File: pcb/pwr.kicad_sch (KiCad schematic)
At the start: 7 parts, among them U2 MCP73831-2-OT

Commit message: sussy
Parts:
- added BT2: Battery_Cell, symbol Device:Battery_Cell
- added C19: 10uF, symbol Device:C_Small
- added C20: 22uF, symbol Device:C_Small
- added C21, C22, C23: 1uF, symbol Device:C_Small
- added C24: 4.7uF, symbol Device:C_Small
- added D2: red, symbol Device:LED_Small
- added D3: green, symbol Device:LED_Small
- added L4: 0.47uH, symbol Device:L_Small
- added R10: 46.4k, symbol Device:R_Small
- added R11: 4.12k, symbol Device:R_Small
- added R12: 10k, symbol Device:R_Small
- added R3: 100k, symbol Device:R_Small
- added R4: 511k, symbol Device:R_Small
- added R5: 91k, symbol Device:R_Small
- added R6, R7: 1.5k, symbol Device:R_Small
- added R8: 1.18k, symbol Device:R_Small
- added R9: 1.13k, symbol Device:R_Small
- added U4: TPS63802DLAR, TPS63802DLAR:VREG_TPS63802DLAR, symbol TPS63802:TPS63802DLAR
- added U5: BQ24074RGT, Package_DFN_QFN:VQFN-16-1EP_3x3mm_P0.5mm_EP1.6x1.6mm, symbol Battery_Management:BQ24074RGT
- added U6: TPS7A20xxxDQN, Package_SON:Texas_X2SON-4_1x1mm_P0.65mm, symbol Regulator_Linear:TPS7A20xxxDQN
- BT1, C1, C16, D1, R1, R2, U2: now not fitted; now left out of the parts list
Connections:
- net GND: now also BT1.2 (-), C1.2, BT2.2 (-), C19.2, C20.2, C21.2, C22.2, C23.2, C24.2, R10.1, R11.1, R12.2, R5.2, R8.1, R9.1, U4.2 (MODE), U4.3 (AGND), U4.8 (GND), U5.17 (VSS), U5.8 (VSS), U6.2 (GND), U6.5 (Pad)
- net VBUS: now also C23.1, U5.13 (IN)
- net at R2.1, U2.5 (PROG): no longer R1.2
- net +BATT: now reaches BT1.1 (+), C1.1, U2.3 (V_{BAT})
- net +BATT: now also C19.1, R3.1, R6.2, R7.2, U4.10 (VIN), U5.10 (OUT), U5.11 (OUT)
- new net: D3.1 (K), U5.7 (~{PGOOD})
- new net: D3.2 (A), R6.1
- new net: R12.1, U5.1 (TS)
- new net: R10.2, U5.14 (TMR)
- new net: R4.2, R5.1, U4.4 (FB)
- new net: R3.2, U4.5 (PG)
- new net: L4.1, U4.7 (L2)
- new net: L4.2, U4.9 (L1)
- new net: D2.1 (K), U5.9 (~{CHG})
- new net: D2.2 (A), R7.1
- new net: R1.2, U2.1 (STAT)
- new net: R8.2, U5.12 (ILIM)
- new net: R11.2, U5.15 (ITERM)
- new net: R9.2, U5.16 (ISET)
- new net: BT2.1 (+), C24.1, U5.2 (BAT), U5.3 (BAT)
- new net +3V0_GPS: C22.1, U6.1 (OUT)
- new net +3V3_ALT: C20.1, C21.1, R4.1, U4.6 (VOUT), U6.4 (IN)
- new net P0.25: U4.1 (EN)
- new net P0.26: U6.3 (EN)
- new net P1.04: U5.4 (~{CE})
- new net P1.05: U5.6 (EN1)
- new net P1.06: U5.5 (EN2)

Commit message: stuff
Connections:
- net VBAT_RAW: now reaches BT2.1 (+), C24.1, U5.2 (BAT), U5.3 (BAT)
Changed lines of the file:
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@@
 	)
 	(junction
+		(at 53.34 96.52)
+		(diameter 0)
+		(color 0 0 0 0)
+	)
+	(junction
 		(at 110.49 96.52)
 		(diameter 0)
@@
 	)
 	(junction
-		(at 66.04 96.52)
-		(diameter 0)
-		(color 0 0 0 0)
-	)
-	(junction
 		(at 96.52 116.84)
 		(diameter 0)
@@
 		)
 	)
+	(global_label "VBAT_RAW"
+		(shape input)
+		(at 231.14 104.14 0)
+		(fields_autoplaced yes)
+		(effects
+			(font
+				(size 1.27 1.27)
+			)
+			(justify left)
+		)
+		(property "Intersheetrefs" "${INTERSHEET_REFS}"
+			(at 243.3176 104.14 0)
+			(hide yes)
+			(show_name no)
+			(do_not_autoplace no)
+			(effects
+				(font
+					(size 1.27 1.27)
+				)
+				(justify left)
+			)
+		)
+	)
 	(global_label "P0.25"
 		(shape input)
@@
 		(in_pos_files yes)
 		(dnp no)
-		(fields_autoplaced yes)
 		(property "Reference" "BT2"
-			(at 234.95 106.1084 0)
+			(at 233.68 106.68 0)
 			(show_name no)
 			(do_not_autoplace no)
@@
 		)
 		(property "Value" "Battery_Cell"
-			(at 234.95 108.6484 0)
+			(at 233.68 109.22 0)
 			(show_name no)
 			(do_not_autoplace no)
@@
 	(symbol
 		(lib_id "power:+BATT")
-		(at 66.04 96.52 0)
+		(at 53.34 96.52 0)
 		(unit 1)
 		(body_style 1)
@@
 		(fields_autoplaced yes)
 		(property "Reference" "#PWR025"
-			(at 66.04 100.33 0)
+			(at 53.34 100.33 0)
 			(hide yes)
 			(show_name no)
@@
 		)
 		(property "Value" "+BATT"
-			(at 66.04 91.44 0)
+			(at 53.34 91.44 0)
 			(show_name no)
 			(do_not_autoplace no)
@@
 		)
 		(property "Footprint" ""
-			(at 66.04 96.52 0)
+			(at 53.34 96.52 0)
 			(hide yes)
 			(show_name no)
@@
 		)
 		(property "Datasheet" ""
-			(at 66.04 96.52 0)
+			(at 53.34 96.52 0)
 			(hide yes)
 			(show_name no)
@@
 		)
 		(property "Description" "Power symbol creates a global label with name \"+BATT\""
-			(at 66.04 96.52 0)
+			(at 53.34 96.52 0)
 			(hide yes)
 			(show_name no)

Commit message: sus commit
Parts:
- BT2: footprint (none) -> Connector_JST:JST_PH_S2B-PH-SM4-TB_1x02-1MP_P2.00mm_Horizontal
- C19: footprint (none) -> Capacitor_SMD:C_0603_1608Metric; LCSC Part (none) -> C96446
- C20: footprint (none) -> Capacitor_SMD:C_0805_2012Metric; LCSC Part (none) -> C45783
- C21, C22, C23: footprint (none) -> Capacitor_SMD:C_0402_1005Metric; LCSC Part (none) -> C52923
- C24: footprint (none) -> Capacitor_SMD:C_0603_1608Metric; LCSC Part (none) -> C19666
- D2: footprint (none) -> LED_SMD:LED_0603_1608Metric; LCSC Part (none) -> C2286
- D3: footprint (none) -> LED_SMD:LED_0805_2012Metric; LCSC Part (none) -> C2297
- L4: footprint (none) -> JLCImport:XFL4015-471MEC
- R10: value 46.4k -> 1.18k; footprint (none) -> Resistor_SMD:R_0402_1005Metric; LCSC Part (none) -> C3016052
- R11: value 4.12k -> 1.13k; footprint (none) -> Resistor_SMD:R_0603_1608Metric; LCSC Part (none) -> C22833
- R12: value 10k -> 46.4k; footprint (none) -> Resistor_SMD:R_0402_1005Metric; LCSC Part (none) -> C5126026
- R3: footprint (none) -> Resistor_SMD:R_0402_1005Metric; LCSC Part (none) -> C25741
- R4: footprint (none) -> Resistor_SMD:R_0603_1608Metric; LCSC Part (none) -> C2930114
- R5: footprint (none) -> Resistor_SMD:R_0402_1005Metric; LCSC Part (none) -> C2906973
- R6, R7: footprint (none) -> Resistor_SMD:R_0402_1005Metric; LCSC Part (none) -> C25867
- R8: value 1.18k -> 1.5k; footprint (none) -> Resistor_SMD:R_0402_1005Metric; LCSC Part (none) -> C25867
- R9: value 1.13k -> 1.5k; footprint (none) -> Resistor_SMD:R_0402_1005Metric; LCSC Part (none) -> C25867
- U4: value TPS63802DLAR -> nRF52840; footprint TPS63802DLAR:VREG_TPS63802DLAR -> Package_DFN_QFN:Nordic_AQFN-73-1EP_7x7mm_P0.5mm; LCSC Part (none) -> C190794; MANUFACTURER Texas Instruments -> (none); MAXIMUM_PACKAGE_HEIGHT 1.0 mm -> (none); PARTREV B -> (none); STANDARD Manufacturer Recommendations -> (none)
- U5: value BQ24074RGT -> MAX-M10S; footprint Package_DFN_QFN:VQFN-16-1EP_3x3mm_P0.5mm_EP1.6x1.6mm -> RF_GPS:ublox_MAX; LCSC Part (none) -> C4153167
- U6: value TPS7A20xxxDQN -> TPS63802DLAR; footprint Package_SON:Texas_X2SON-4_1x1mm_P0.65mm -> TPS63802DLAR:VREG_TPS63802DLAR; LCSC Part (none) -> C2845237; MANUFACTURER (none) -> Texas Instruments; MAXIMUM_PACKAGE_HEIGHT (none) -> 1.0 mm; PARTREV (none) -> B; STANDARD (none) -> Manufacturer Recommendations

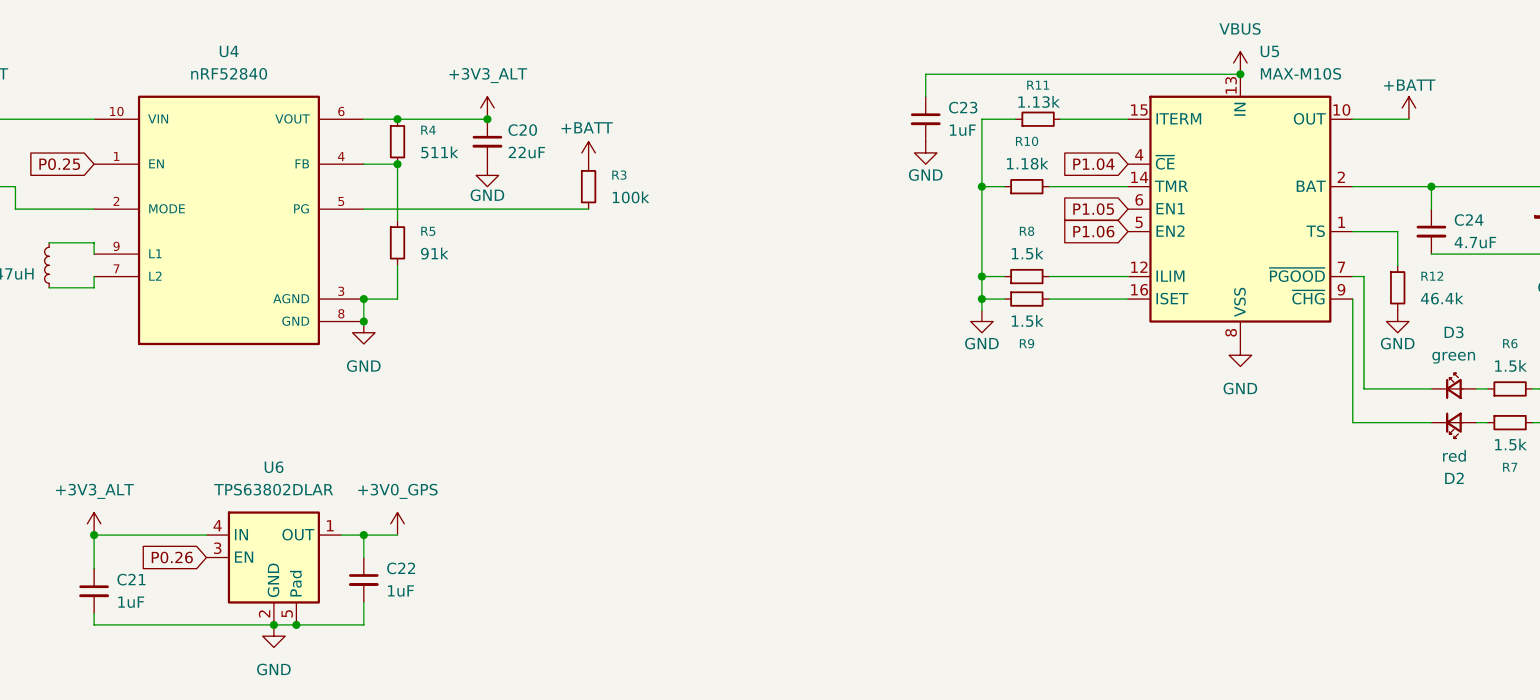
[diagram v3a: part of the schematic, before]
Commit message: fix symbols getting absolutely goofed up
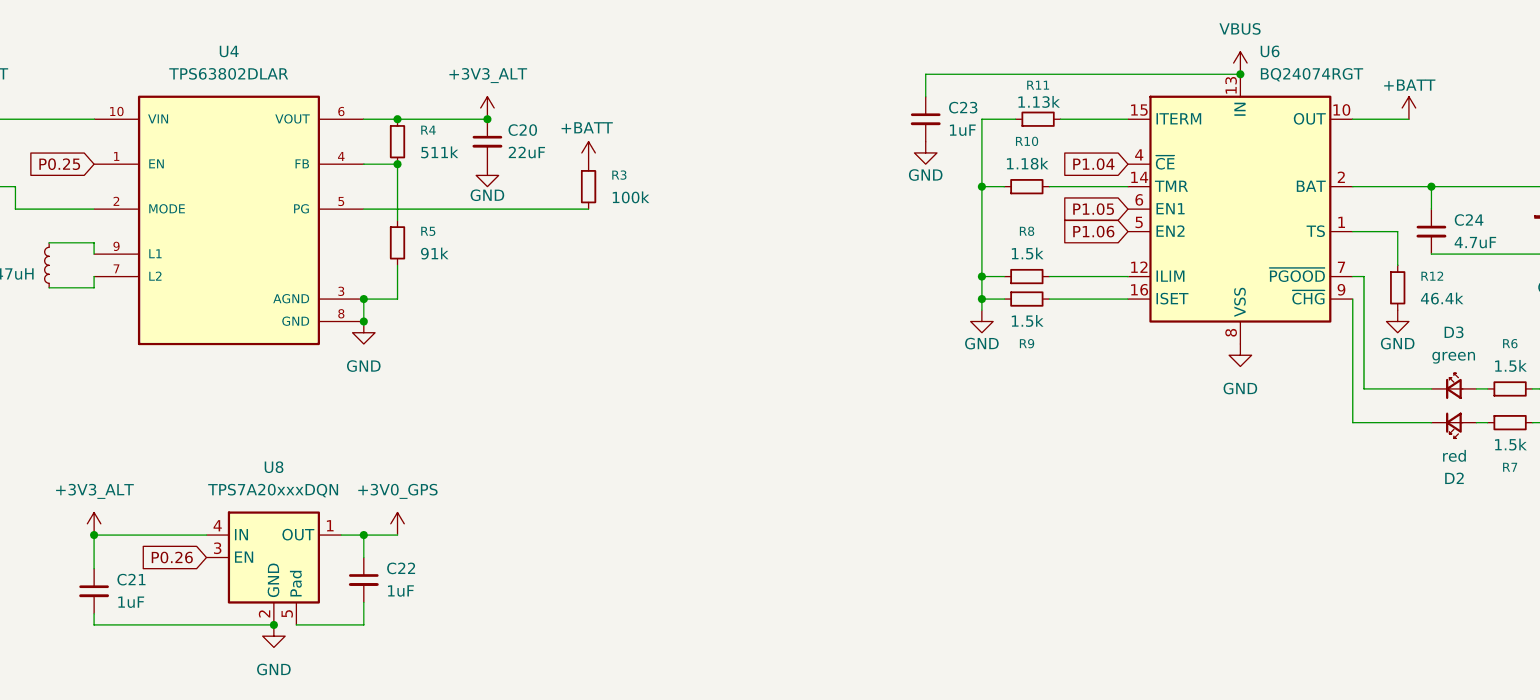
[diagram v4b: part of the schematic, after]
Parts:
- removed U5: MAX-M10S, RF_GPS:ublox_MAX, symbol Battery_Management:BQ24074RGT
- removed U6: TPS63802DLAR, TPS63802DLAR:VREG_TPS63802DLAR, symbol Regulator_Linear:TPS7A20xxxDQN
- added U6: BQ24074RGT, Package_DFN_QFN:VQFN-16-1EP_3x3mm_P0.5mm_EP1.6x1.6mm, symbol Battery_Management:BQ24074RGT
- added U8: TPS7A20xxxDQN, Package_SON:Texas_X2SON-4_1x1mm_P0.65mm, symbol Regulator_Linear:TPS7A20xxxDQN
- U4: value nRF52840 -> TPS63802DLAR; footprint Package_DFN_QFN:Nordic_AQFN-73-1EP_7x7mm_P0.5mm -> TPS63802DLAR:VREG_TPS63802DLAR; LCSC Part C190794 -> (none); MANUFACTURER (none) -> Texas Instruments; MAXIMUM_PACKAGE_HEIGHT (none) -> 1.0 mm; PARTREV (none) -> B; STANDARD (none) -> Manufacturer Recommendations
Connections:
- net +3V0_GPS: now also U8.1 (OUT)
- net +3V3_ALT: now also U8.4 (IN)
- net +BATT: now also U6.10 (OUT), U6.11 (OUT)
- net GND: now also U6.17 (VSS), U6.8 (VSS), U8.2 (GND); no longer C22.2
- net P0.26: now also U8.3 (EN)
- net P1.04: now also U6.4 (~{CE})
- net P1.05: now also U6.6 (EN1)
- net P1.06: now also U6.5 (EN2)
- net VBAT_RAW: now also U6.2 (BAT), U6.3 (BAT)
- net VBUS: now also U6.13 (IN)
- net at D3.1 (K): now also U6.7 (~{PGOOD})
- net at R12.1: now also U6.1 (TS)
- net at R10.2: now also U6.14 (TMR)
- net at D2.1 (K): now also U6.9 (~{CHG})
- net at R8.2: now also U6.12 (ILIM)
- net at R11.2: now also U6.15 (ITERM)
- net at R9.2: now also U6.16 (ISET)
- new net: C22.2, U8.5 (Pad)

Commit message: ALMOST done with parts purgatory
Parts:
- BT2: LCSC Part (none) -> C295747
- U4: LCSC Part (none) -> C2845237
- U6: LCSC Part (none) -> C54313
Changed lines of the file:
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@@
 			)
 		)
+		(property "LCSC Part" "C54313"
+			(at 195.58 106.68 0)
+			(hide yes)
+			(show_name no)
+			(do_not_autoplace no)
+			(effects
+				(font
+					(size 1.27 1.27)
+				)
+			)
+		)
 		(pin "11"
 		)
@@
 			)
 		)
+		(property "LCSC Part" "C2845237"
+			(at 81.28 106.68 0)
+			(hide yes)
+			(show_name no)
+			(do_not_autoplace no)
+			(effects
+				(font
+					(size 1.27 1.27)
+				)
+			)
+		)
 		(pin "9"
 		)
@@
 			(at 231.14 109.22 0)
 			(hide yes)
+			(show_name no)
+			(do_not_autoplace no)
+			(effects
+				(font
+					(size 1.27 1.27)
+				)
+			)
+		)
+		(property "LCSC Part" "C295747"
+			(at 231.14 109.22 0)
+			(hide yes)

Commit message: sussy
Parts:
- removed BT2: Battery_Cell, Connector_JST:JST_PH_S2B-PH-SM4-TB_1x02-1MP_P2.00mm_Horizontal, symbol Device:Battery_Cell
- added BT1: Battery_Cell, Connector_JST:JST_PH_S2B-PH-SM4-TB_1x02-1MP_P2.00mm_Horizontal, symbol Device:Battery_Cell
- added SW6: PWR, JLCImport:SK-3296S-01-L1, symbol Switch:SW_SPDT
- U4: footprint TPS63802DLAR:VREG_TPS63802DLAR -> JLCImport:TPS63802DLAR
- renumbered BT1 to BT2, C19 to C17, C21 to C18, C22 to C19, C23 to C21, C24 to C22, C16 to C23, C1 to C24, D3 to D1, D1 to D3, R12 to R10, R6 to R11, R7 to R12, R1 to R13, R2 to R14, R4 to R3, R5 to R4, R3 to R5, R10 to R6, R8 to R7, R9 to R8, R11 to R9, U8 to U5, U2 to U7
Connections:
- net GND: now also BT1.2 (-)
- net VBAT_RAW: now also SW6.1 (A)
- new net: BT1.1 (+), SW6.2 (B)
- no-connect marks 0 -> 1
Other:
- moved on the sheet: C17, C18, C19, C20, C21, C22, D1, D2, L4, R10, R11, R12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

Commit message: amogus
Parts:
- added J2: Adafruit Wireless Chg Module, Connector_PinHeader_2.54mm:PinHeader_1x02_P2.54mm_Vertical, symbol Connector:Conn_01x02_Socket
- added R17: 10k, Resistor_SMD:R_0402_1005Metric, symbol Device:R
- added U9: TPS2116DRL, Package_TO_SOT_SMD:SOT-583-8, symbol Power_Management:TPS2116DRL
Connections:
- net GND: now also J2.1 (Pin_1), U9.1 (GND)
- net VBUS: now also U9.3 (VIN1), U9.4 (PR1), U9.5 (MODE); no longer C21.1, U6.13 (IN)
- new net: J2.2 (Pin_2), U9.6 (VIN2)
- new net +3V3: R17.1
- new net P1.15: R17.2, U9.8 (ST)
- new net V_CHARGE: C21.1, U6.13 (IN), U9.2 (VOUT), U9.7 (VOUT)
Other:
- moved on the sheet: BT1, C17, C18, C19, C20, C21, C22, D1, D2, L4, R10, R11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
